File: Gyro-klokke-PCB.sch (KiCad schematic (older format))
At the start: 18 parts, among them J1 Conn_01x04_Male, J2 Conn_01x04_Male, J3 Conn_01x03_Male, SW1 SW_Push, SW2 SW_Push, U1 STM32F030F4Px, U2 LB1948MC, U3 LB1948MC, Y1 Crystal_Small

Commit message: Kretskort ferdig v1.0
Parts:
- added C3, C4: C_Small, Capacitor_SMD:C_0603_1608Metric, symbol Device:C_Small
- added C5: 100nF, Capacitor_SMD:C_0805_2012Metric, symbol Device:C_Small
- added J4: Conn_02x05_Odd_Even, Connector_PinHeader_1.27mm:PinHeader_2x05_P1.27mm_Vertical_SMD, symbol Connector_Generic:Conn_02x05_Odd_Even
- added J5, J6: Conn_01x01_Female, MountingHole:MountingHole_2.2mm_M2_ISO14580_Pad, symbol Connector:Conn_01x01_Female
- J3: footprint Connector_Molex:Molex_PicoBlade_53398-0371_1x03-1MP_P1.25mm_Vertical -> Connector_Molex:Molex_PicoBlade_53398-0471_1x04-1MP_P1.25mm_Vertical; symbol Connector:Conn_01x03_Male -> Connector:Conn_01x04_Male
- SW1, SW2: footprint Button_Switch_SMD:SW_Push_1P1T_NO_6x6mm_H9.5mm -> Button_Switch_SMD:SW_SPST_EVQP7A
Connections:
- net labels added: SWD-SWCLK, SWD-SWIO, nRESET
- wire segments 79 -> 102
- no-connect marks 0 -> 5

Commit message: før nrf52
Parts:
- C3, C4: value C_Small -> 6pF
- R1: value R_Small -> 47R
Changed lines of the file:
@@
 P 2850 2800
 F 0 "R1" H 2909 2846 50  0000 L CNN
-F 1 "R_Small" H 2909 2755 50  0000 L CNN
+F 1 "47R" H 2909 2755 50  0000 L CNN
 F 2 "Resistor_SMD:R_0603_1608Metric" H 2850 2800 50  0001 C CNN
 F 3 "~" H 2850 2800 50  0001 C CNN
@@
 P 3200 3250
 F 0 "C3" V 2971 3250 50  0000 C CNN
-F 1 "C_Small" V 3062 3250 50  0000 C CNN
+F 1 "6pF" V 3062 3250 50  0000 C CNN
 F 2 "Capacitor_SMD:C_0603_1608Metric" H 3200 3250 50  0001 C CNN
 F 3 "~" H 3200 3250 50  0001 C CNN
@@
 P 3200 3450
 F 0 "C4" V 2971 3450 50  0000 C CNN
-F 1 "C_Small" V 3062 3450 50  0000 C CNN
+F 1 "6pF" V 3062 3450 50  0000 C CNN
 F 2 "Capacitor_SMD:C_0603_1608Metric" H 3200 3450 50  0001 C CNN
 F 3 "~" H 3200 3450 50  0001 C CNN

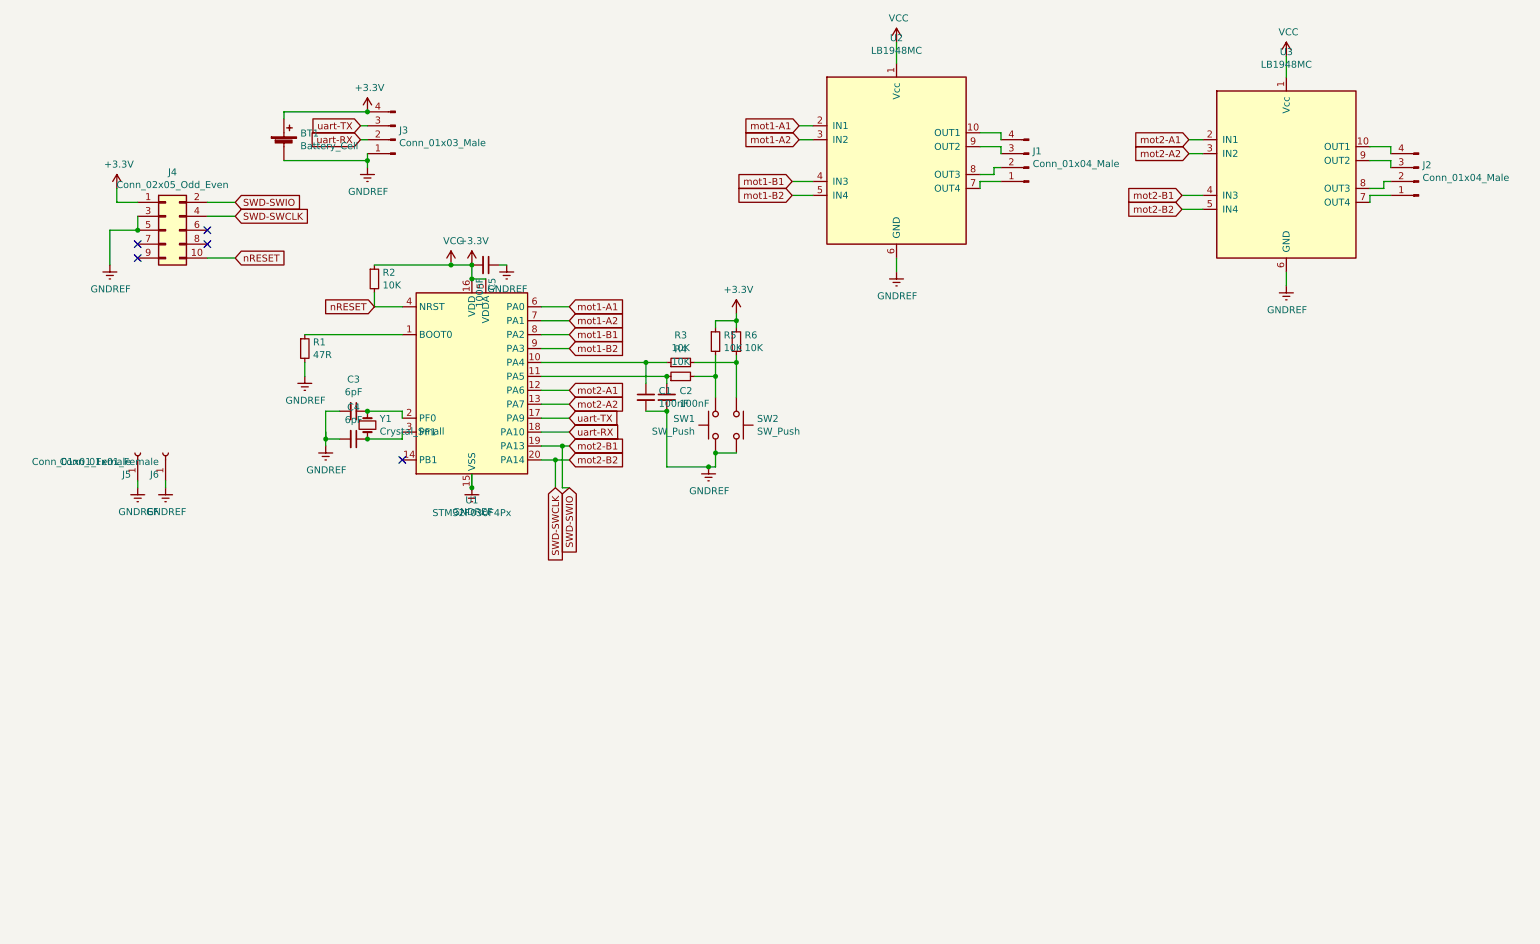
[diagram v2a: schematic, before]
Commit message: endret stm32 til nrf
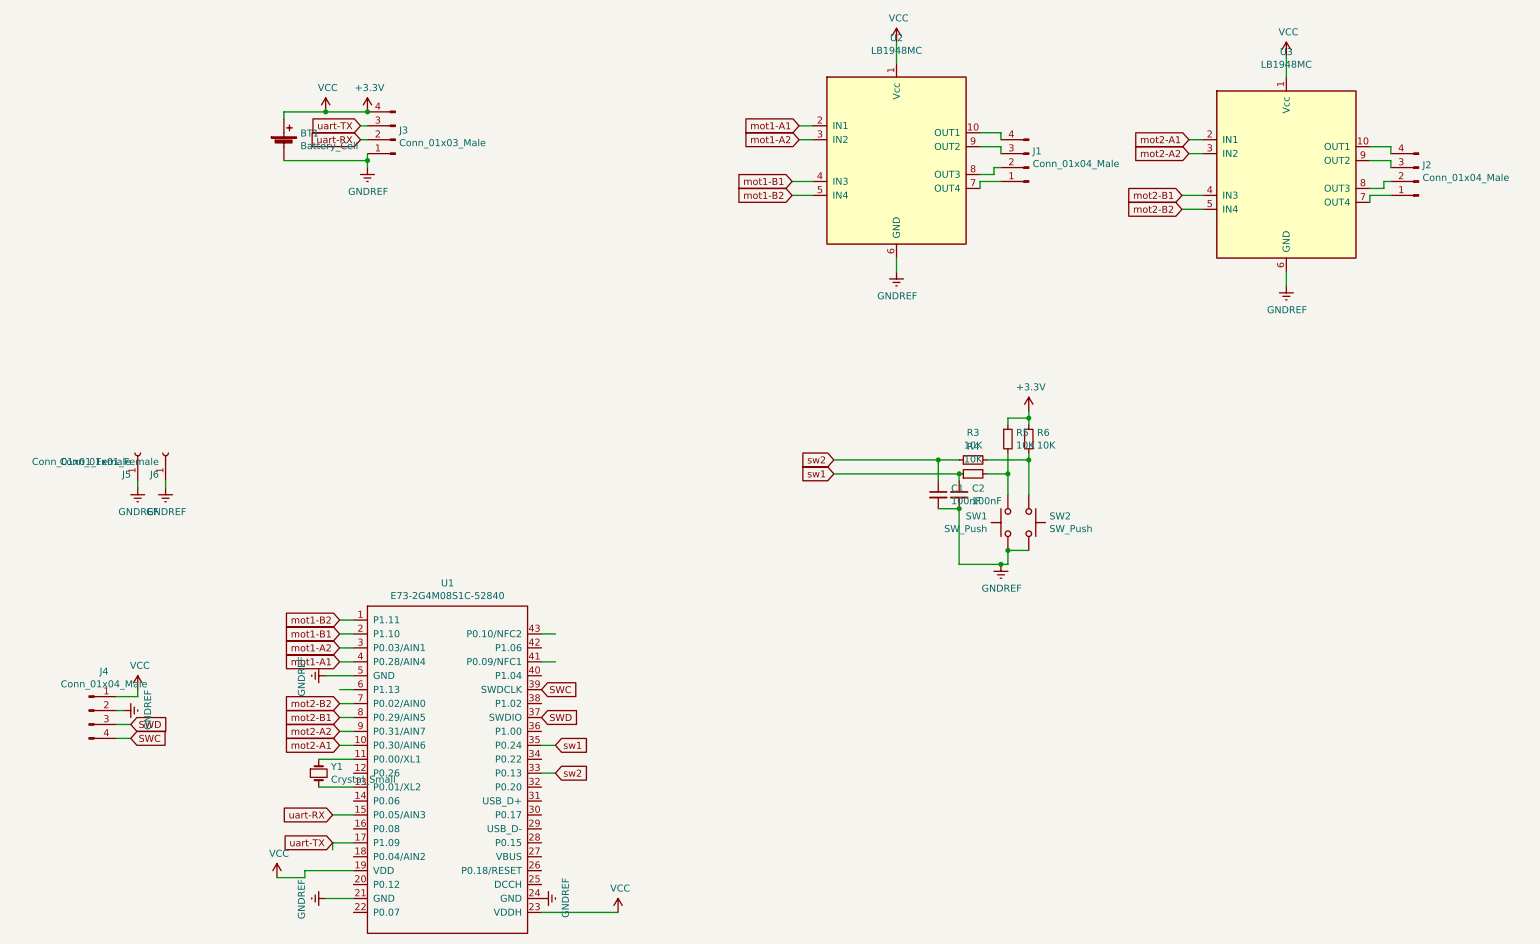
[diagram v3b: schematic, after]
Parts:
- removed C3, C4: 6pF, Capacitor_SMD:C_0603_1608Metric, symbol Device:C_Small
- removed C5: 100nF, Capacitor_SMD:C_0805_2012Metric, symbol Device:C_Small
- removed J4: Conn_02x05_Odd_Even, Connector_PinHeader_1.27mm:PinHeader_2x05_P1.27mm_Vertical_SMD, symbol Connector_Generic:Conn_02x05_Odd_Even
- removed R1: 47R, Resistor_SMD:R_0603_1608Metric, symbol Device:R_Small
- removed R2: 10K, Resistor_SMD:R_0603_1608Metric, symbol Device:R_Small
- removed U1: STM32F030F4Px, Package_SO:TSSOP-20_4.4x6.5mm_P0.65mm, symbol MCU_ST_STM32F0:STM32F030F4Px
- added J4: Conn_01x04_Male, Connector_PinHeader_1.27mm:PinHeader_1x04_P1.27mm_Vertical, symbol Connector:Conn_01x04_Male
- added U1: E73-2G4M08S1C-52840, nrfmicro:E73-2G4M08S1C-52840, symbol nrfmicro:E73-2G4M08S1C-52840
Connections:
- net labels added: SWC, SWD, sw1, sw2
- net labels removed: SWD-SWCLK, SWD-SWIO, nRESET
- wire segments 102 -> 90
- no-connect marks 5 -> 0
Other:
- moved on the sheet: C1, C2, R3, R4, R5, R6, SW1, SW2, Y1

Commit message: Fikset ting
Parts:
- removed J3: Conn_01x03_Male, Connector_Molex:Molex_PicoBlade_53398-0471_1x04-1MP_P1.25mm_Vertical, symbol Connector:Conn_01x04_Male
- added J7: USB_C_Receptacle_USB2.0, nrfmicro:USB-C_C168688, symbol nrfmicro:USB_C_Receptacle_USB2.0
- added J8: Conn_01x02_Female, Connector_PinHeader_1.27mm:PinHeader_2x01_P1.27mm_Vertical, symbol Connector:Conn_01x02_Female
- added R1, R2: 5.7K, Resistor_SMD:R_0603_1608Metric, symbol Device:R_Small
- U1: symbol nrfmicro:E73-2G4M08S1C-52840 -> Gyro-klokke-PCB-rescue:E73-2G4M08S1C-52840-nrfmicro
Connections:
- net labels added: D+, D-, VBUS
- wire segments 90 -> 110
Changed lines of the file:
@@
 	9200 1300 9300 1300
-$Comp
-L Connector:Conn_01x04_Male J3
-U 1 1 5FC5C45F
-P 3500 1300
-F 0 "J3" H 3472 1232 50  0000 R CNN
-F 1 "Conn_01x03_Male" H 3472 1323 50  0000 R CNN
-F 2 "Connector_Molex:Molex_PicoBlade_53398-0471_1x04-1MP_P1.25mm_Vertical" H 3500 1300 50  0001 C CNN
-F 3 "~" H 3500 1300 50  0001 C CNN
-	1    3500 1300
-	-1   0    0    1
-$EndComp
 $Comp
 L power:+3.3V #PWR0110
@@
 Wire Wire Line
 	3300 1400 3300 1450
-Text GLabel 3250 1200 0    50   Input ~ 0
-uart-TX
-Wire Wire Line
-	3250 1300 3300 1300
 $Comp
 L Device:Crystal_Small Y1
@@
 Wire Wire Line
 	2700 1100 2700 1150
-Connection ~ 3300 1100
-Text GLabel 3250 1300 0    50   Input ~ 0
-uart-RX
-Wire Wire Line
-	3250 1200 3300 1200
 $Comp
 L Connector:Conn_01x01_Female J6
@@
 	3000 5150 3200 5150
 $Comp
-L nrfmicro:E73-2G4M08S1C-52840 U1
+L Gyro-klokke-PCB-rescue:E73-2G4M08S1C-52840-nrfmicro U1
 U 1 1 60A5065E
 P 3900 5850
@@
 	1650 5300 1650 5250
 $Comp
-L power:VCC #PWR?
+L power:VCC #PWR02
 U 1 1 60B2C84F
 P 3000 1100
-F 0 "#PWR?" H 3000 950 50  0001 C CNN
+F 0 "#PWR02" H 3000 950 50  0001 C CNN
 F 1 "VCC" H 3015 1273 50  0000 C CNN
 F 2 "" H 3000 1100 50  0001 C CNN
@@
 Wire Wire Line
 	3000 1100 2700 1100
+$Comp
+L nrfmicro:USB_C_Receptacle_USB2.0 J7
+U 1 1 60E6A41F
+P 1200 1700
+F 0 "J7" H 1307 2567 50  0000 C CNN
+F 1 "USB_C_Receptacle_USB2.0" H 1307 2476 50  0000 C CNN
+F 2 "nrfmicro:USB-C_C168688" H 1350 1700 50  0001 C CNN
+F 3 "" H 1350 1700 50  0001 C CNN
+	1    1200 1700
+	1    0    0    -1
+$EndComp
+Text Label 1800 1100 0    50   ~ 0
+VBUS
+Text Label 2000 1600 0    50   ~ 0
+D-
+Text Label 2000 1800 0    50   ~ 0
+D+
+$Comp
+L power:GNDREF #PWR01
+U 1 1 60E74F5B
+P 1050 2800
+F 0 "#PWR01" H 1050 2550 50  0001 C CNN
+F 1 "GNDREF" H 1055 2627 50  0000 C CNN
+F 2 "" H 1050 2800 50  0001 C CNN
+F 3 "" H 1050 2800 50  0001 C CNN
+	1    1050 2800
+	1    0    0    -1
+$EndComp
+Wire Wire Line
+	900  2600 900  2700
+Wire Wire Line
+	900  2700 1050 2700
+Wire Wire Line
+	1050 2700 1050 2800
+Wire Wire Line
+	1050 2700 1200 2700
+Wire Wire Line
+	1200 2700 1200 2600
+Connection ~ 1050 2700
+Wire Wire Line
+	1800 1900 1900 1900
+Wire Wire Line
+	1900 1900 1900 1800
+Wire Wire Line
+	1900 1800 2000 1800
+Wire Wire Line
+	1800 1800 1900 1800
+Connection ~ 1900 1800
+Wire Wire Line
+	1800 1700 1900 1700
+Wire Wire Line
+	1900 1700 1900 1600
+Wire Wire Line
+	1900 1600 2000 1600
+Wire Wire Line
+	1800 1600 1900 1600
+Connection ~ 1900 1600
+Text Label 4650 6250 0    50   ~ 0
+D-
+Text Label 4650 6050 0    50   ~ 0
+D+
+Text Label 4900 6350 0    50   ~ 0
+VBUS
+Wire Wire Line
+	4550 6050 4650 6050
+Wire Wire Line
+	4650 6250 4550 6250
+Wire Wire Line
+	5150 6450 4550 6450
+$Comp
+L Connector:Conn_01x02_Female J8
+U 1 1 60EC4861
+P 5350 6350
+F 0 "J8" H 5378 6326 50  0000 L CNN
+F 1 "Conn_01x02_Female" H 5378 6235 50  0000 L CNN
+F 2 "Connector_PinHeader_1.27mm:PinHeader_2x01_P1.27mm_Vertical" H 5350 6350 50  0001 C CNN
+F 3 "~" H 5350 6350 50  0001 C CNN
+	1    5350 6350
+	1    0    0    -1
+$EndComp
+Wire Wire Line
+	4900 6350 5150 6350
+$Comp
+L Device:R_Small R1
+U 1 1 60ED462E
+P 1900 1300
+F 0 "R1" V 1704 1300 50  0000 C CNN
+F 1 "5.7K" V 1795 1300 50  0000 C CNN
+F 2 "Resistor_SMD:R_0603_1608Metric" H 1900 1300 50  0001 C CNN
+F 3 "~" H 1900 1300 50  0001 C CNN
+	1    1900 1300
+	0    1    1    0
+$EndComp
+$Comp
+L Device:R_Small R2
+U 1 1 60ED58CD
+P 2200 1400
+F 0 "R2" V 2004 1400 50  0000 C CNN
+F 1 "5.7K" V 2095 1400 50  0000 C CNN
+F 2 "Resistor_SMD:R_0603_1608Metric" H 2200 1400 50  0001 C CNN
+F 3 "~" H 2200 1400 50  0001 C CNN
+	1    2200 1400
+	0    1    1    0
+$EndComp
+$Comp
+L power:GNDREF #PWR03
+U 1 1 60ED9E3B
+P 2400 1500
+F 0 "#PWR03" H 2400 1250 50  0001 C CNN
+F 1 "GNDREF" H 2405 1327 50  0000 C CNN
+F 2 "" H 2400 1500 50  0001 C CNN
+F 3 "" H 2400 1500 50  0001 C CNN
+	1    2400 1500
+	1    0    0    -1
+$EndComp
+Wire Wire Line
+	2000 1300 2400 1300
+Wire Wire Line
+	2400 1300 2400 1400
+Wire Wire Line
+	1800 1400 2100 1400
+Wire Wire Line
+	2300 1400 2400 1400
+Connection ~ 2400 1400
+Wire Wire Line
+	2400 1400 2400 1500
 $EndSCHEMATC
